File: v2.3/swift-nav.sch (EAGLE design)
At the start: 156 parts, among them J1 SMA_EDGE, J6 ZX62-B-5PA, Q1 IRLML6401, U1 6SLX9FTG256, U10 MAX2769, U12 PT7M8206B33TA5EX, U13 M25PX80, U2 LTC3407A_DFN, U3 STM32-M-64-LQFP, U4 7Q-16.368MBG-T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

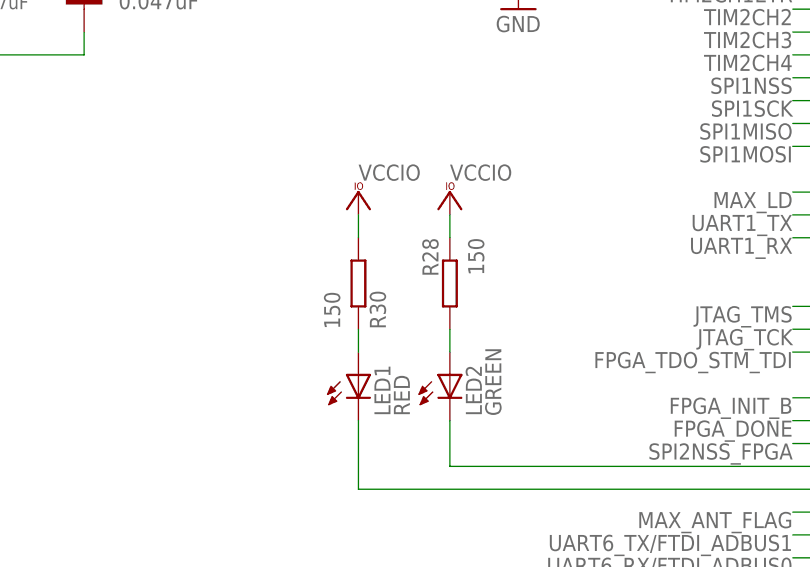
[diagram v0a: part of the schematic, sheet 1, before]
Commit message: Changed some RF matching inductor values and the red LED resistor value
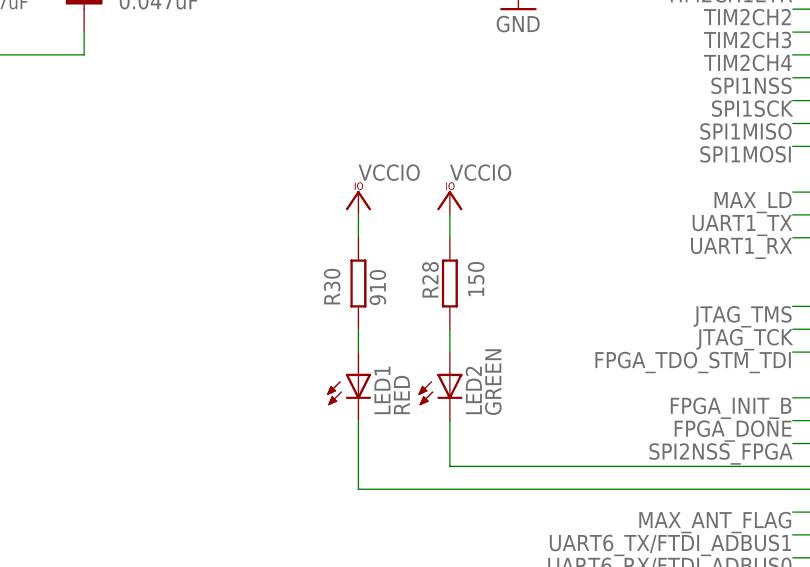
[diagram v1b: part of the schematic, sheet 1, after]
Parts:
- L1: value 29nH / DNP -> 27nH / DNP
- L2: value 29nH -> 27nH
- L3: value 29nH -> 3.3nH
- L5: value 3.3nH -> 2nH
- R30: value 150 -> 910
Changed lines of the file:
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@@
 <setting verticaltext="up"/>
 </settings>
-<grid distance="0.1" unitdist="inch" unit="inch" style="lines" multiple="1" display="yes" altdistance="0.01" altunitdist="inch" altunit="inch"/>
+<grid distance="0.1" unitdist="inch" unit="inch" style="lines" multiple="1" display="no" altdistance="0.01" altunitdist="inch" altunit="inch"/>
 <layers>
 <layer number="1" name="Top" color="4" fill="1" visible="no" active="no"/>
@@
 <part name="R28" library="pel_dipol_comp" deviceset="RESISTOR" device="-0402" value="150"/>
 <part name="VCC13" library="supply1" deviceset="VCCIO" device=""/>
-<part name="R30" library="pel_dipol_comp" deviceset="RESISTOR" device="-0402" value="150"/>
+<part name="R30" library="pel_dipol_comp" deviceset="RESISTOR" device="-0402" value="910"/>
 <part name="VCC28" library="supply1" deviceset="VCCIO" device=""/>
 <part name="LED1" library="pel_dipol_comp" deviceset="LED" device="-0603" value="RED"/>
@@
 <part name="C20" library="pel_dipol_comp" deviceset="CAPACITOR" device="-0402" value="0.047uF"/>
 <part name="GND23" library="supply1" deviceset="GND" device=""/>
-<part name="L2" library="pel_dipol_comp" deviceset="INDUCTOR" device="-0402" value="29nH"/>
+<part name="L2" library="pel_dipol_comp" deviceset="INDUCTOR" device="-0402" value="27nH"/>
 <part name="C37" library="pel_dipol_comp" deviceset="CAPACITOR" device="-0402" value="100pF"/>
 <part name="C38" library="pel_dipol_comp" deviceset="CAPACITOR" device="-0402" value="12pF"/>
@@
 <part name="C12" library="pel_dipol_comp" deviceset="CAPACITOR" device="-0402" value="100pF"/>
 <part name="C13" library="pel_dipol_comp" deviceset="CAPACITOR" device="-0402" value="0.47uF"/>
-<part name="L1" library="pel_dipol_comp" deviceset="INDUCTOR" device="-0402" value="29nH / DNP"/>
-<part name="L3" library="pel_dipol_comp" deviceset="INDUCTOR" device="-0402" value="29nH"/>
+<part name="L1" library="pel_dipol_comp" deviceset="INDUCTOR" device="-0402" value="27nH / DNP"/>
+<part name="L3" library="pel_dipol_comp" deviceset="INDUCTOR" device="-0402" value="3.3nH"/>
 <part name="R12" library="pel_dipol_comp" deviceset="RESISTOR" device="-0402" value="10k"/>
 <part name="VCC37" library="supply1" deviceset="VCCIO" device=""/>
@@
 <part name="X3" library="pel_molex" deviceset="CONN_12-1" device="-53261" value="FPGA DEBUG"/>
 <part name="L4" library="pel_dipol_comp" deviceset="INDUCTOR" device="-0402" value="5.1nH"/>
-<part name="L5" library="pel_dipol_comp" deviceset="INDUCTOR" device="-0402" value="3.3nH"/>
+<part name="L5" library="pel_dipol_comp" deviceset="INDUCTOR" device="-0402" value="2nH"/>
 <part name="GND62" library="supply1" deviceset="GND" device=""/>
 <part name="C36" library="pel_dipol_comp" deviceset="CAPACITOR" device="-0402" value="100pF"/>
@@
 <attribute name="VALUE" x="59.69" y="163.83" size="1.778" layer="96"/>
 </instance>
-<instance part="R28" gate="G$1" x="119.38" y="116.84" rot="R270"/>
+<instance part="R28" gate="G$1" x="119.38" y="116.84" smashed="yes" rot="R270">
+<attribute name="VALUE" x="121.412" y="119.38" size="1.778" layer="96" rot="R270"/>
+<attribute name="NAME" x="116.332" y="119.38" size="1.778" layer="95" rot="R270"/>
+</instance>
 <instance part="VCC13" gate="G$1" x="119.38" y="127" smashed="yes">
 <attribute name="VALUE" x="119.38" y="128.27" size="1.778" layer="96"/>
 </instance>
-<instance part="R30" gate="G$1" x="109.22" y="116.84" rot="R90"/>
+<instance part="R30" gate="G$1" x="109.22" y="116.84" smashed="yes" rot="R90">
+<attribute name="VALUE" x="112.268" y="114.3" size="1.778" layer="96" rot="R90"/>
+<attribute name="NAME" x="107.188" y="114.3" size="1.778" layer="95" rot="R90"/>
+</instance>
 <instance part="VCC28" gate="G$1" x="109.22" y="127" smashed="yes">
 <attribute name="VALUE" x="109.22" y="128.27" size="1.778" layer="96"/>

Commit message: Changed revisions numbers from 2.3 to 2.3.1
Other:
- note added: "2.3.1"
- note removed: "2.3"
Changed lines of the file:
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@@
 <text x="203.2" y="187.96" size="5.08" layer="94">STM32F4</text>
 <text x="330.2" y="27.94" size="5.08" layer="94">Microcontroller</text>
-<text x="424.18" y="10.16" size="3.81" layer="94" rot="R180">2.3</text>
+<text x="426.72" y="10.16" size="3.81" layer="94" rot="R180">2.3.1</text>
 <text x="105.41" y="171.45" size="2.54" layer="97">Reset Button</text>
 <text x="40.64" y="185.42" size="2.1844" layer="97">STM has internal pull-up</text>
@@
 <text x="203.2" y="69.85" size="6.4516" layer="94">Spartan Configuration Flash</text>
 <text x="162.56" y="256.54" size="6.4516" layer="94">Spartan IO Banks</text>
-<text x="205.74" y="228.6" size="2.54" layer="94">Bank 2</text>
-<text x="27.94" y="229.87" size="2.54" layer="94">Bank 0</text>
-<text x="121.92" y="246.38" size="2.54" layer="94">Bank 1</text>
-<text x="353.06" y="245.11" size="2.54" layer="94">Bank 3</text>
+<text x="210.82" y="223.52" size="2.54" layer="94">Bank 2</text>
+<text x="27.94" y="224.79" size="2.54" layer="94">Bank 0</text>
+<text x="124.46" y="243.84" size="2.54" layer="94">Bank 1</text>
+<text x="358.14" y="242.57" size="2.54" layer="94">Bank 3</text>
 <text x="256.286" y="213.868" size="1.778" layer="97">2K4 max for CCLK = 2MHz (default)</text>
 <text x="50.546" y="211.328" size="1.778" layer="97">Short in CONF guide,</text>
@@
 <text x="228.346" y="119.888" size="1.778" layer="97">but 2K is fine</text>
 <text x="281.686" y="119.888" size="1.778" layer="97">Can probably DNP as this is driven by STM</text>
-<text x="424.18" y="10.16" size="3.81" layer="94" rot="R180">2.3</text>
+<text x="426.72" y="10.16" size="3.81" layer="94" rot="R180">2.3.1</text>
 <text x="332.74" y="25.4" size="5.08" layer="94">FPGA IO / JTAG / FLASH</text>
 <text x="63.5" y="54.61" size="6.4516" layer="94">Spartan JTAG</text>
@@
 <text x="149.86" y="86.36" size="2.54" layer="97">Spartan 6 Bypass - Bank 2</text>
 <text x="175.26" y="25.4" size="5.08" layer="94">FPGA Power Pins / Bypassing</text>
-<text x="271.78" y="10.16" size="3.81" layer="94" rot="R180">2.3</text>
+<text x="274.32" y="10.16" size="3.81" layer="94" rot="R180">2.3.1</text>
 </plain>
 <instances>
@@
 <text x="132.08" y="238.76" size="6.4516" layer="94">RF Frontend - Analog Section</text>
 <text x="367.665" y="233.045" size="2.54" layer="94">3V3_RF</text>
-<text x="424.18" y="10.16" size="3.81" layer="94" rot="R180">2.3</text>
+<text x="426.72" y="10.16" size="3.81" layer="94" rot="R180">2.3.1</text>
 <text x="330.2" y="25.4" size="5.08" layer="94">RF Frontend / RF Power</text>
 <text x="294.64" y="243.84" size="6.4516" layer="94">RF LDO Regulator</text>
@@
 <text x="118.745" y="144.145" size="3.81" layer="94">Digital 3V3 and 1V2</text>
 <text x="91.44" y="127" size="1.778" layer="97">Any low Rdson</text>
-<text x="271.78" y="10.16" size="3.81" layer="94" rot="R180">2.3</text>
+<text x="274.32" y="10.16" size="3.81" layer="94" rot="R180">2.3.1</text>
 <text x="180.34" y="25.4" size="5.08" layer="94">Digital Power</text>
 </plain>
@@
 <text x="298.45" y="151.13" size="1.778" layer="97">Insert resistor in UART6_TX to avoid FIFO/UART contention?</text>
 <text x="220.98" y="71.247" size="1.778" layer="97">(1%)</text>
-<text x="424.18" y="10.16" size="3.81" layer="94" rot="R180">2.3</text>
+<text x="426.72" y="10.16" size="3.81" layer="94" rot="R180">2.3.1</text>
 <text x="330.2" y="25.4" size="5.08" layer="94">FTDI UART/FIFO to USB</text>
 </plain>
@@
 <text x="15.24" y="154.94" size="5.08" layer="91" rot="MR180">UART1</text>
 <text x="15.24" y="106.68" size="5.08" layer="91" rot="MR180">UART3</text>
-<text x="269.24" y="10.16" size="3.81" layer="94" rot="R180">2.3</text>
+<text x="274.32" y="10.16" size="3.81" layer="94" rot="R180">2.3.1</text>
 <text x="175.26" y="25.4" size="5.08" layer="94">Connectors / Misc</text>
 <text x="194.945" y="132.08" size="5.08" layer="91">Mounting Holes</text>

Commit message: Cleaned up text in schematic a bit
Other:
- note added: "Could DNP as this is driven by STM"
- note added: "Digital 3V3 / 1V2 Power Rails"
- note added: "Logo"
- note added: "Pulls up IO's during configuration"
- note added: "Route FB lines away from SW lines so they don't feedback"
- note added: "STM32F4 Microcontroller"
- note added: "Short in CONF guide, but 2K is fine"
- note removed: "Any low Rdson"
- note removed: "Can probably DNP as this is driven by STM"
- note removed: "Digital 3V3 and 1V2"
- note removed: "Insert resistor in UART6_TX to avoid FIFO/UART contention?"
- note removed: "Route FB line away from SW line"
- note removed: "STM32F4"
- note removed: "Short in CONF guide,"
- moved on the sheet: R15, R17, R18
